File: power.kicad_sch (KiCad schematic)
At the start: 26 parts, among them J14 Molex_Nano-Fit_1x2_105309-1202, Q1 AO3401A, SW1 SW_EG1218, U4 AP62301_TSOT

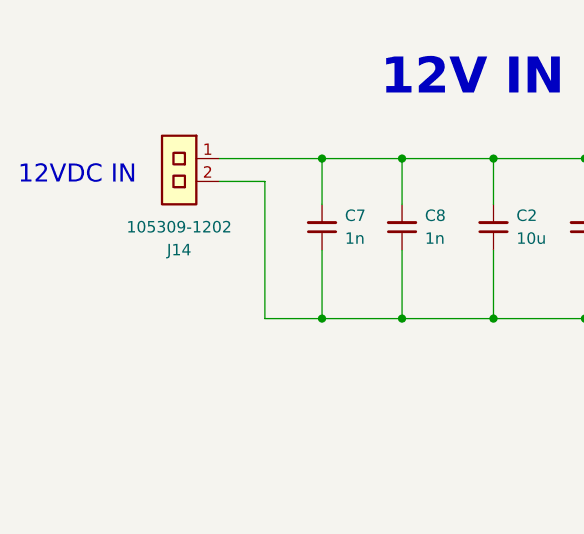
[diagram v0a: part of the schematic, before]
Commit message: [#92504] Update Annotation for connectors
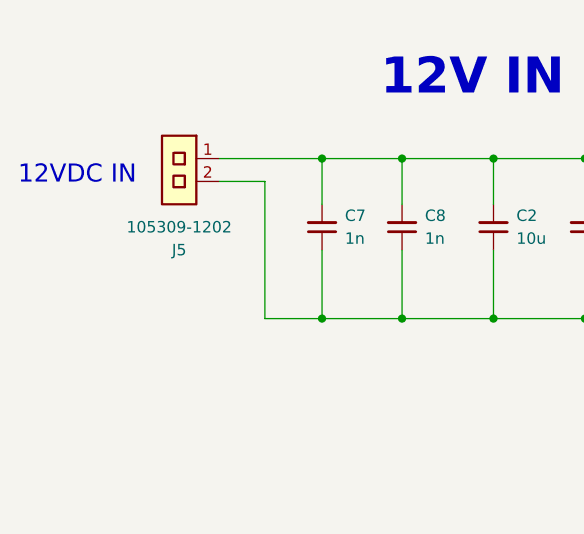
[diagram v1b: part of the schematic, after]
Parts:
- renumbered J14 to J5
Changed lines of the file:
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@@
 		(on_board yes)
 		(dnp no)
-		(property "Reference" "J14"
+		(property "Reference" "J5"
 			(at 67.945 83.82 0)
 			(effects
@@
 			(project ""
 				(path "/5d67ef28-5805-4f87-b722-2926dabf7f6e/6a40469a-13ae-4d69-8a2b-3c10ffcd9800"
-					(reference "J14")
+					(reference "J5")
 					(unit 1)
 				)

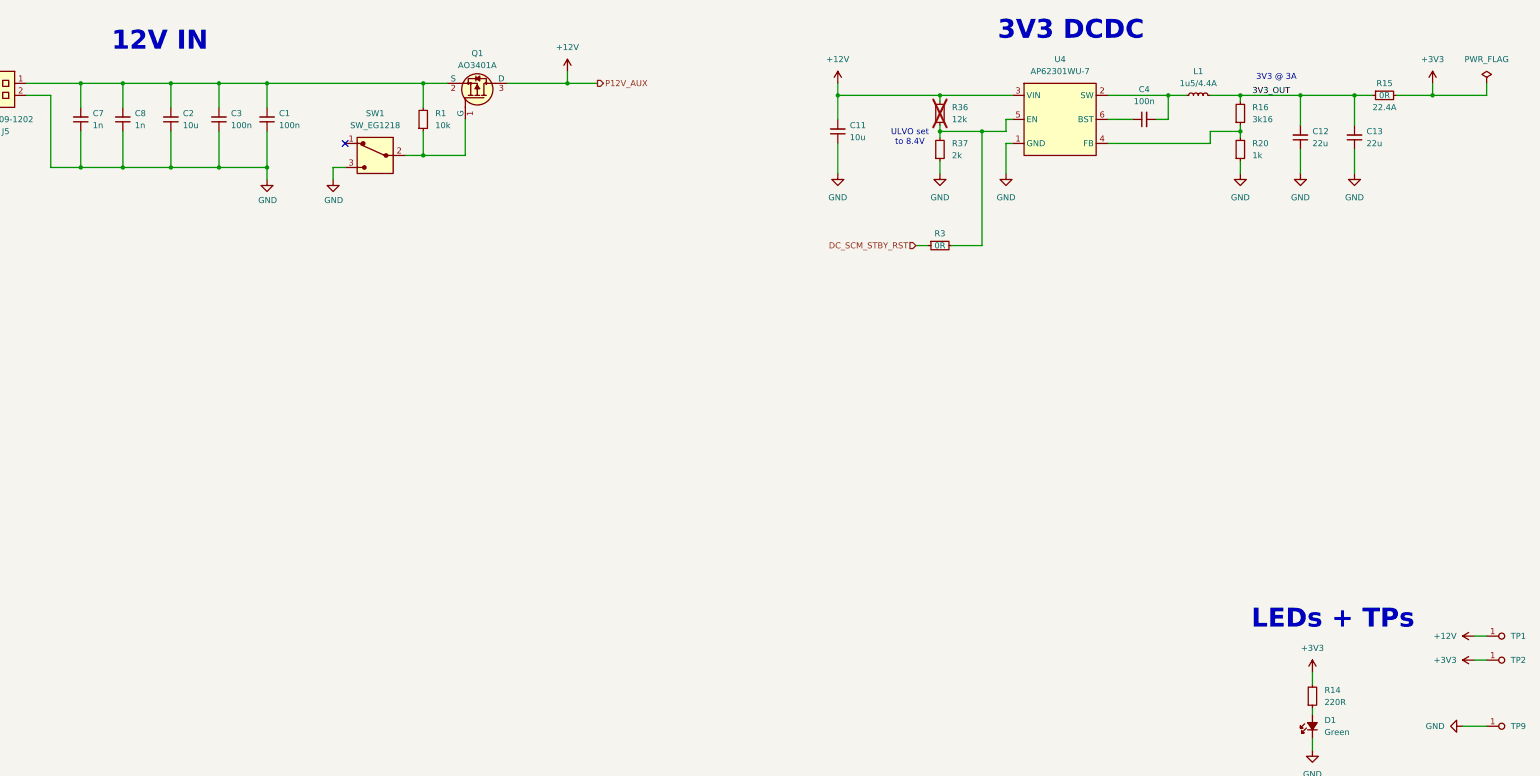
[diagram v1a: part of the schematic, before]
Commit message: [#93090] Add FTDI LDO
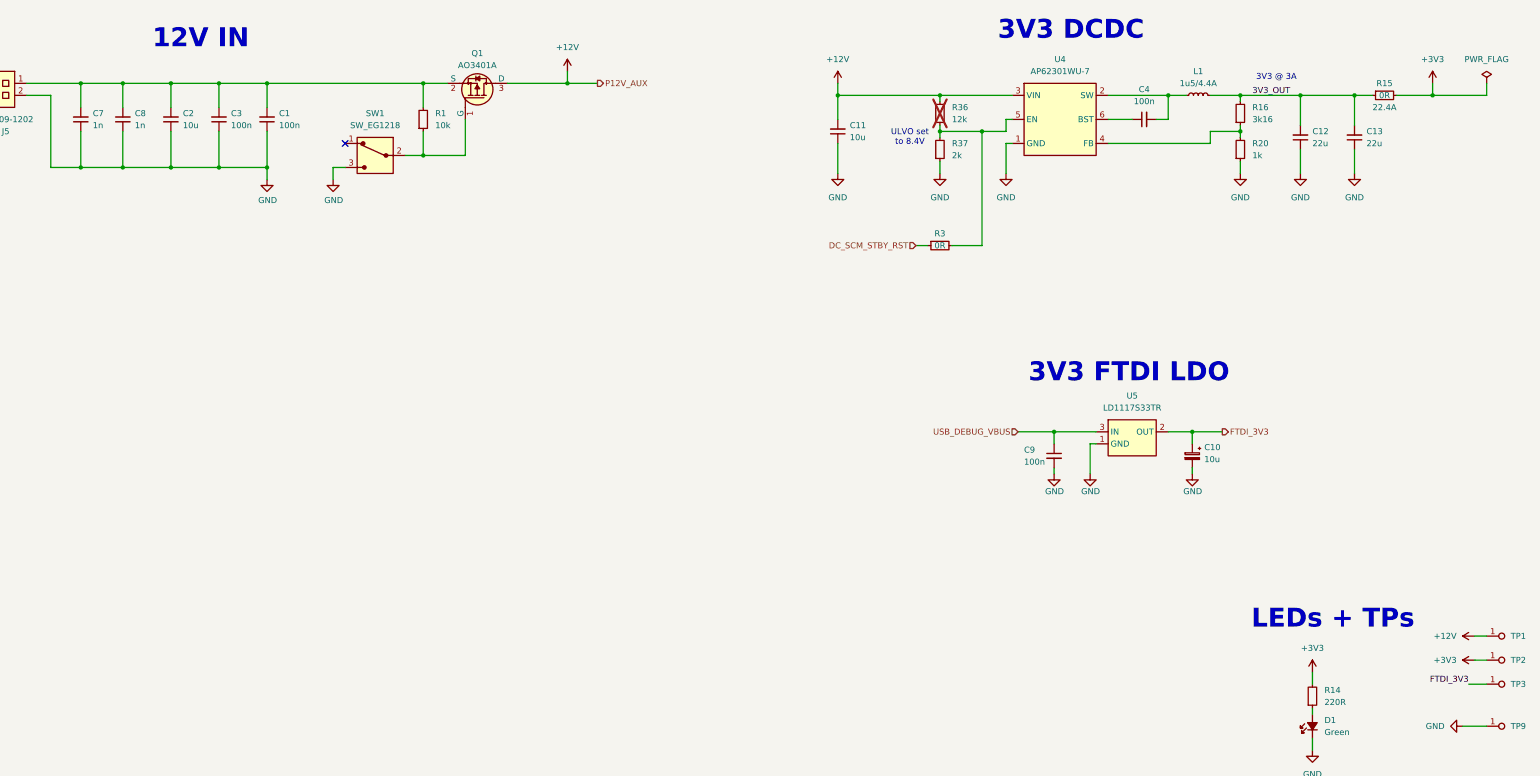
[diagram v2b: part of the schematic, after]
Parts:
- added C10: C_Pol_10u_16V_KEMET-T491-A, antmicro-footprints:C_Pol_EIA-A, symbol antmicroCapacitorspol:C_Pol_10u_16V_KEMET-T491-A
- added C9: C_100n_16V_X7R_0402, antmicro-footprints:C_0402_1005Metric, symbol antmicroCapacitors0402:C_100n_16V_X7R_0402
- added TP3: TP_0.75mm_SMD, antmicro-footprints:TP_SMD_0.75mm, symbol antmicroTestPoints:TP_0.75mm_SMD
- added U5: LD1117S33TR, antmicro-footprints:SOT-223, symbol antmicroPMICVoltageRegulatorsLinear:LD1117S33TR
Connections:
- net GND: now also C10.2, C9.2, U5.1 (GND)
- new net FTDI_3V3: C10.1, TP3.1, U5.2 (OUT), U5.4 (OUT)
- new net USB_DEBUG_VBUS: C9.1, U5.3 (IN)
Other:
- note added: "3V3 FTDI LDO"

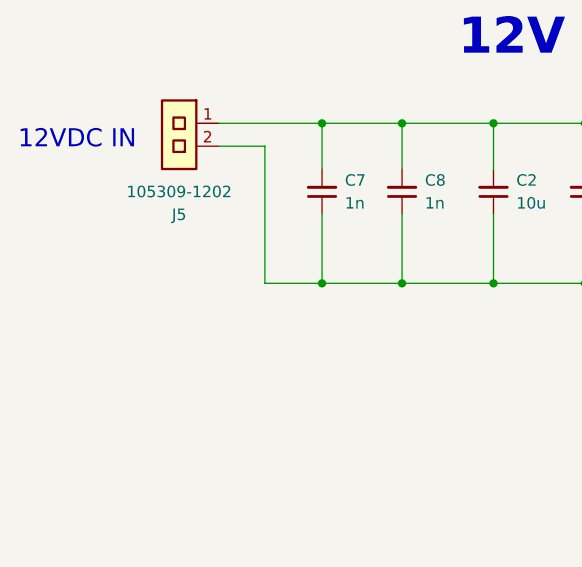
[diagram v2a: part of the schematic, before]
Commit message: [#93090] Change Antmicro Logo and finish 3V3 FTDI power schematic
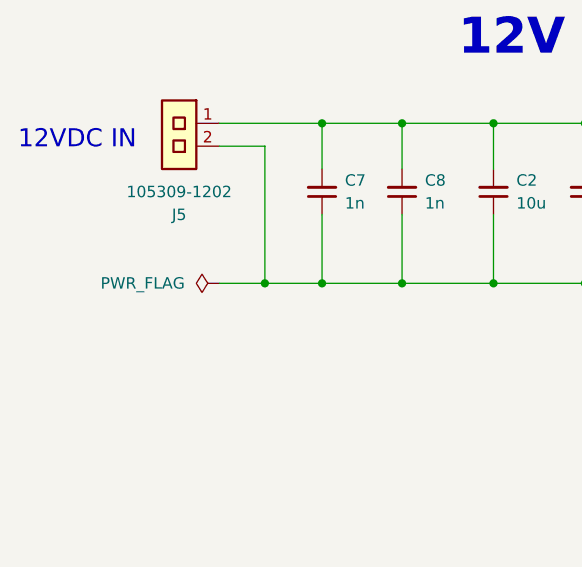
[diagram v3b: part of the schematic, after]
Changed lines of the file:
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@@
 	)
 	(junction
+		(at 77.47 91.44)
+		(diameter 0)
+		(color 0 0 0 0)
+	)
+	(junction
 		(at 289.56 147.32)
 		(diameter 0)
@@
 	(wire
 		(pts
+			(xy 72.39 91.44) (xy 77.47 91.44)
+		)
+		(stroke
+			(width 0)
+			(type default)
+		)
+	)
+	(wire
+		(pts
 			(xy 123.19 73.66) (xy 156.21 73.66)
 		)
@@
 					(unit 1)
 				)
+			)
+		)
+	)
+	(symbol
+		(lib_id "antmicropower:PWR_FLAG")
+		(at 72.39 91.44 90)
+		(unit 1)
+		(exclude_from_sim no)
+		(in_bom yes)
+		(on_board yes)
+		(dnp no)
+		(fields_autoplaced yes)
+		(property "Reference" "#FLG011"
+			(at 70.485 91.44 0)
+			(effects
+				(font
+					(size 1.27 1.27)
+				)
+				(hide yes)
+			)
+		)
+		(property "Value" "PWR_FLAG"
+			(at 68.58 91.4399 90)
+			(effects
+				(font
+					(size 1.27 1.27)
+				)
+				(justify left)
+			)
+		)
+		(property "Footprint" ""
+			(at 72.39 91.44 0)
+			(effects
+				(font
+					(size 1.27 1.27)
+				)
+				(hide yes)
+			)
+		)
+		(property "Datasheet" ""
+			(at 72.39 91.44 0)
+			(effects
+				(font
+					(size 1.27 1.27)
+				)
+				(hide yes)
+			)
+		)
+		(property "Description" ""
+			(at 74.93 91.44 0)
+			(effects
+				(font
+					(size 1.27 1.27)
+				)
+				(justify left bottom)
+				(hide yes)
+			)
+		)
+		(pin "1"
+		)
+		(instances
+			(project ""
+				(path "/5d67ef28-5805-4f87-b722-2926dabf7f6e/6a40469a-13ae-4d69-8a2b-3c10ffcd9800"
+					(reference "#FLG011")
+					(unit 1)
+				)

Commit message: [#93514] Propagate title and date across all of the sheets
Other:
- title: DC-SCM Carrier Card for OSM-L SoMs -> Datacenter Secure Control Module Breakout Board
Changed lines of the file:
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@@
 	(paper "A3")
 	(title_block
-		(title "DC-SCM Carrier Card for OSM-L SoMs")
-		(date "2025-10-14")
-		(rev "1.1.0")
+		(title "Datacenter Secure Control Module Breakout Board")
+		(date "2021-12-16")
+		(rev "2.0.0")
 	)
 	(text "12VDC IN"

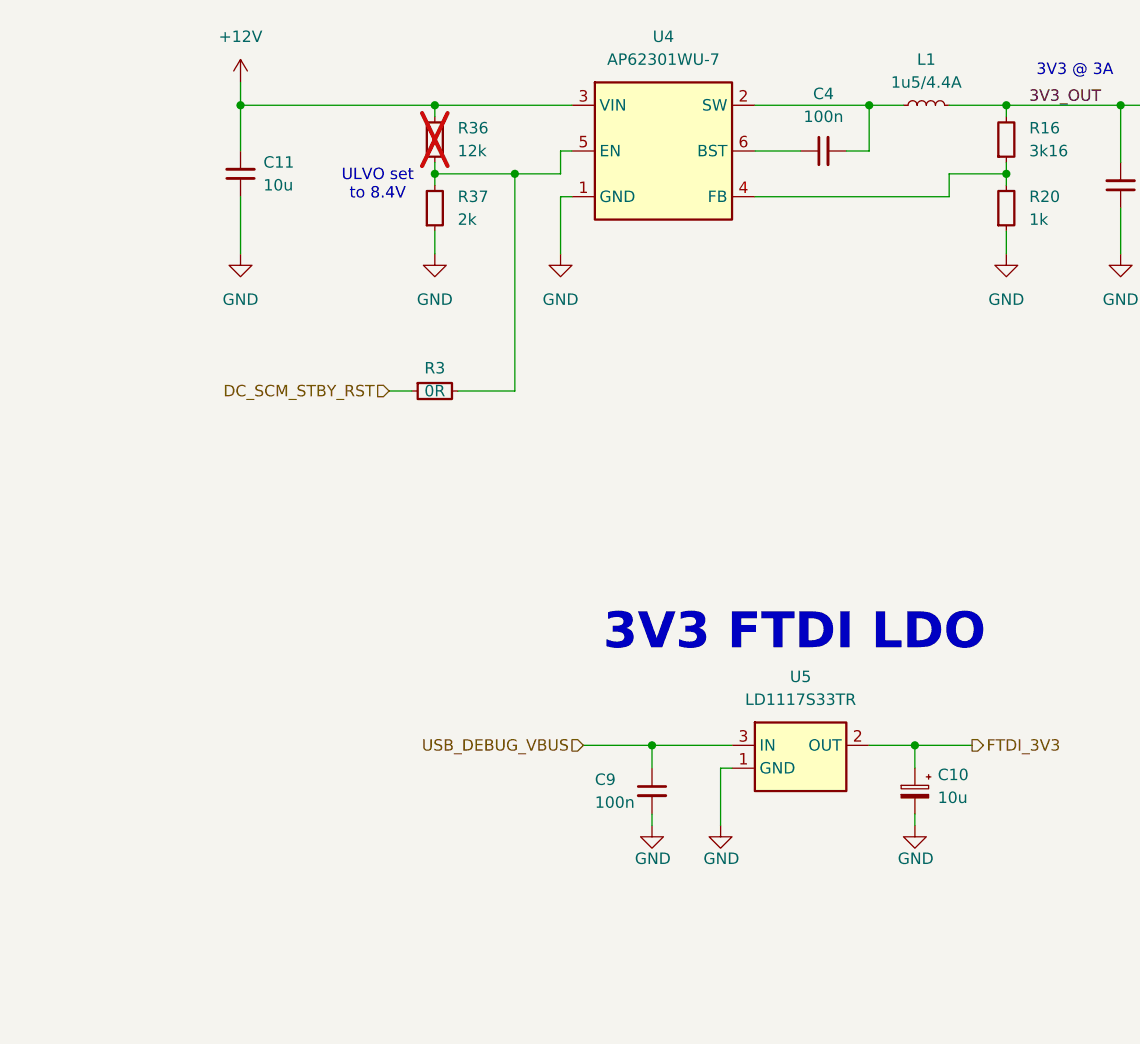
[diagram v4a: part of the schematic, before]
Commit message: [#93514] Remove UVLO note and added marked DC_SCM_STBY_RST properly
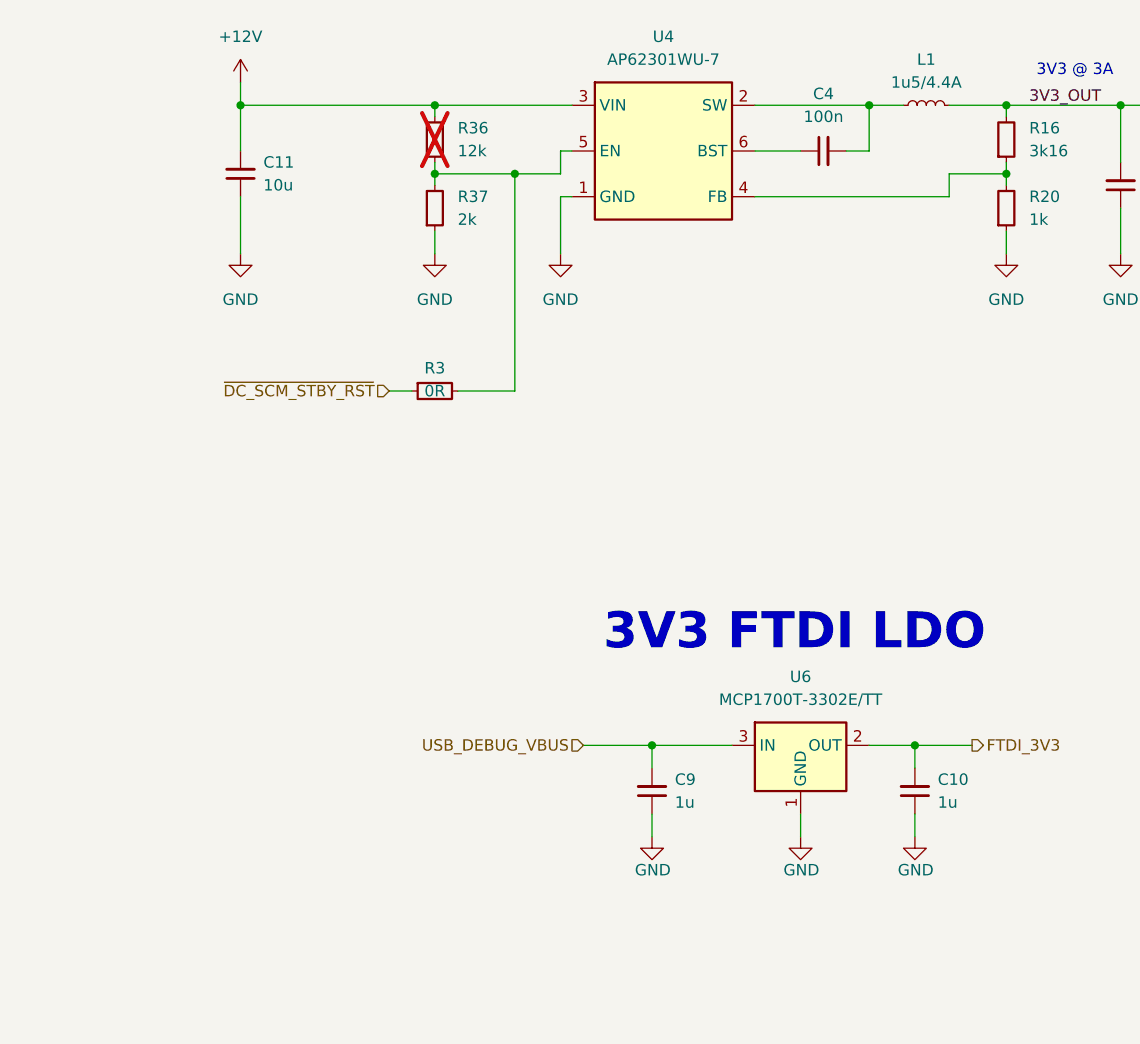
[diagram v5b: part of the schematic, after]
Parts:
- removed C10: C_Pol_10u_16V_KEMET-T491-A, antmicro-footprints:C_Pol_EIA-A, symbol antmicroCapacitorspol:C_Pol_10u_16V_KEMET-T491-A
- removed C9: C_100n_16V_X7R_0402, antmicro-footprints:C_0402_1005Metric, symbol antmicroCapacitors0402:C_100n_16V_X7R_0402
- removed U5: LD1117S33TR, antmicro-footprints:SOT-223, symbol antmicroPMICVoltageRegulatorsLinear:LD1117S33TR
- added C10, C9: C_1u_10V_X7R_0402, antmicro-footprints:C_0402_1005Metric, symbol antmicroCapacitors0402:C_1u_10V_X7R_0402
- added U6: MCP1700T-3302E_TT, antmicro-footprints:SOT-23-3, symbol antmicroPMICVoltageRegulatorsLinear:MCP1700T-3302E_TT
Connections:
- net FTDI_3V3: now also C10.2, U6.2 (OUT)
- net GND: now also C10.1, C9.1, U6.1 (GND)
- net USB_DEBUG_VBUS: now also C9.2, U6.3 (IN)
- net DC_SCM_STBY_RST renamed ~{DC_SCM_STBY_RST}
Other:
- note removed: "ULVO set to 8.4V"

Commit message: [#93514] Add separating lines, clean schematics
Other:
- moved on the sheet: C10, C9, D1, R14, TP1, TP2, TP3, TP9, U6
